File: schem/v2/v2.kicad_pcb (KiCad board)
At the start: 2 copper layers, 97 x 86 mm, 3 parts, among them U1 DOIT-ESP32-DEVKIT-V1

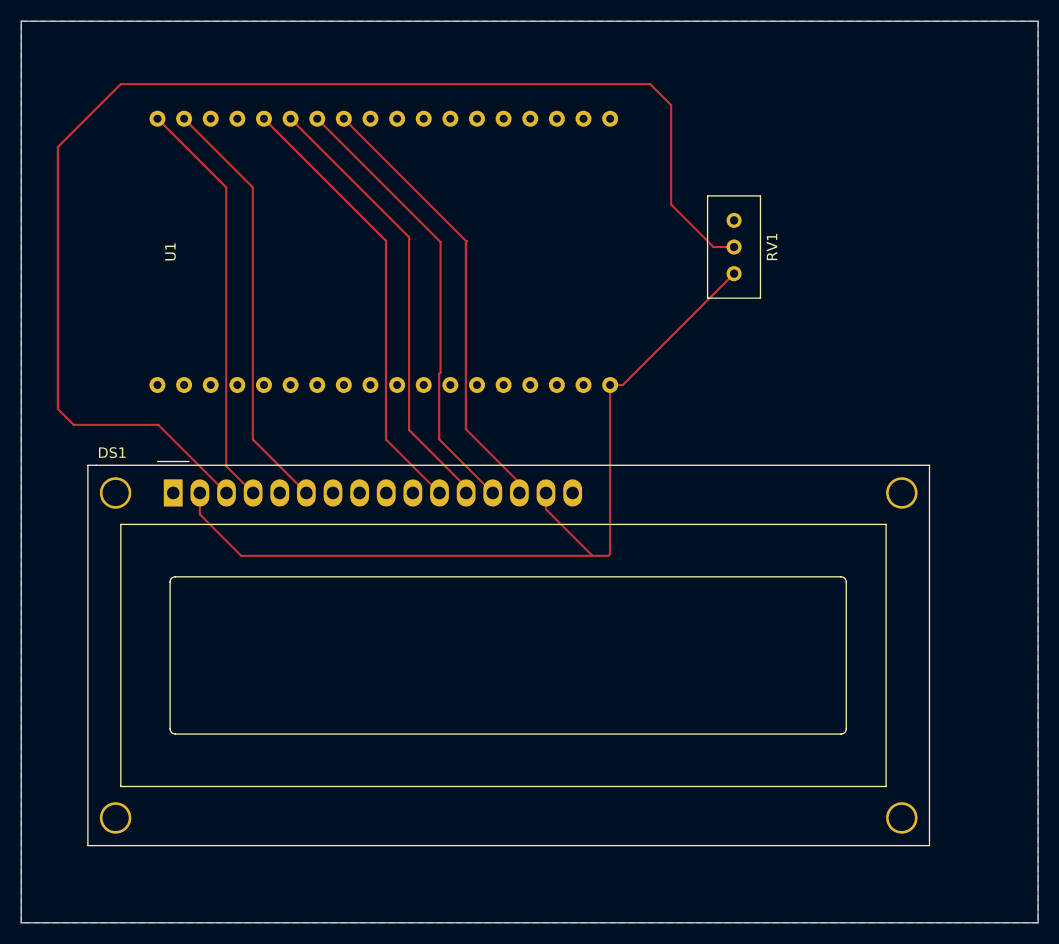
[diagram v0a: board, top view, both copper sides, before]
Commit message: added v3 double sided WIP
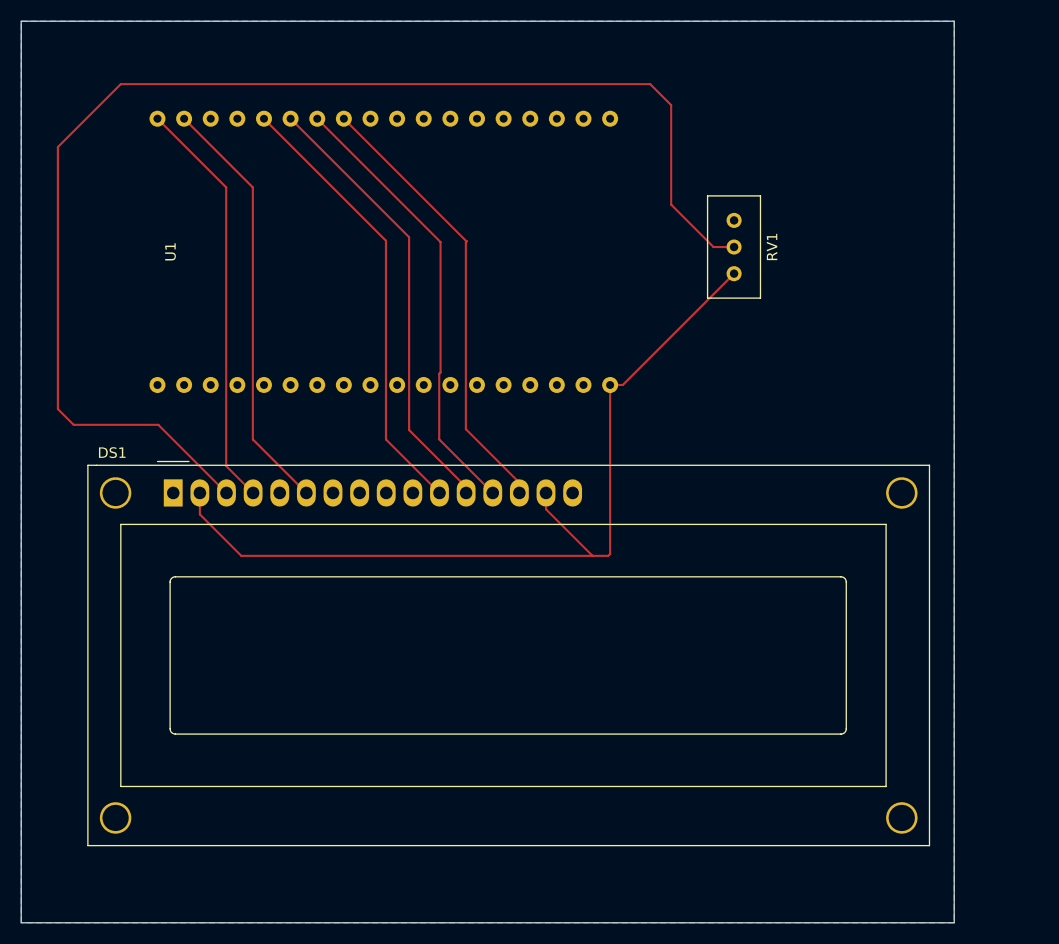
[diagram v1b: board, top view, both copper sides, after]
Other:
- board size 97 x 86 mm -> 89 x 86 mm
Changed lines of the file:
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@@
 	(gr_rect
 		(start 178.5 31)
-		(end 275.5 117)
+		(end 267.5 117)
 		(stroke
 			(width 0.05)
@@
 		(polygon
 			(pts
-				(xy 178.5 31) (xy 275.5 31) (xy 275.5 117) (xy 178.5 117)
+				(xy 178.5 31) (xy 267.5 31) (xy 267.5 117) (xy 178.5 117)
 			)
 		)
+	)
+	(zone
+		(net 0)
+		(net_name "")
+		(layer "B.Cu")
+		(hatch edge 0.5)
+		(connect_pads
+			(clearance 0)
+		)
+		(min_thickness 0.25)
+		(filled_areas_thickness no)
+		(keepout
+			(tracks not_allowed)
+			(vias not_allowed)
+			(pads not_allowed)
+			(copperpour not_allowed)
+			(footprints allowed)
+		)
+		(placement
+			(enabled no)
+			(sheetname "/")
+		)
+		(fill
+			(thermal_gap 0.5)
+			(thermal_bridge_width 0.5)
+		)
+		(polygon
+			(pts
+				(xy 196.5 44) (xy 188.5 44) (xy 188.5 63) (xy 196.5 63)
+			)
+		)
